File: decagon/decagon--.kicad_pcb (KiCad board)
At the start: 2 copper layers, 161.7 x 153.8 mm, 39 parts, among them J1 Conn_01x05_Pin, J10 Conn_01x05_Pin, J2 Conn_01x05_Pin, J3 Conn_01x05_Pin, J4 Conn_01x05_Pin, J5 Conn_01x05_Pin, J6 Conn_01x05_Pin, J7 Conn_01x05_Pin, J8 Conn_01x05_Pin, J9 Conn_01x05_Pin

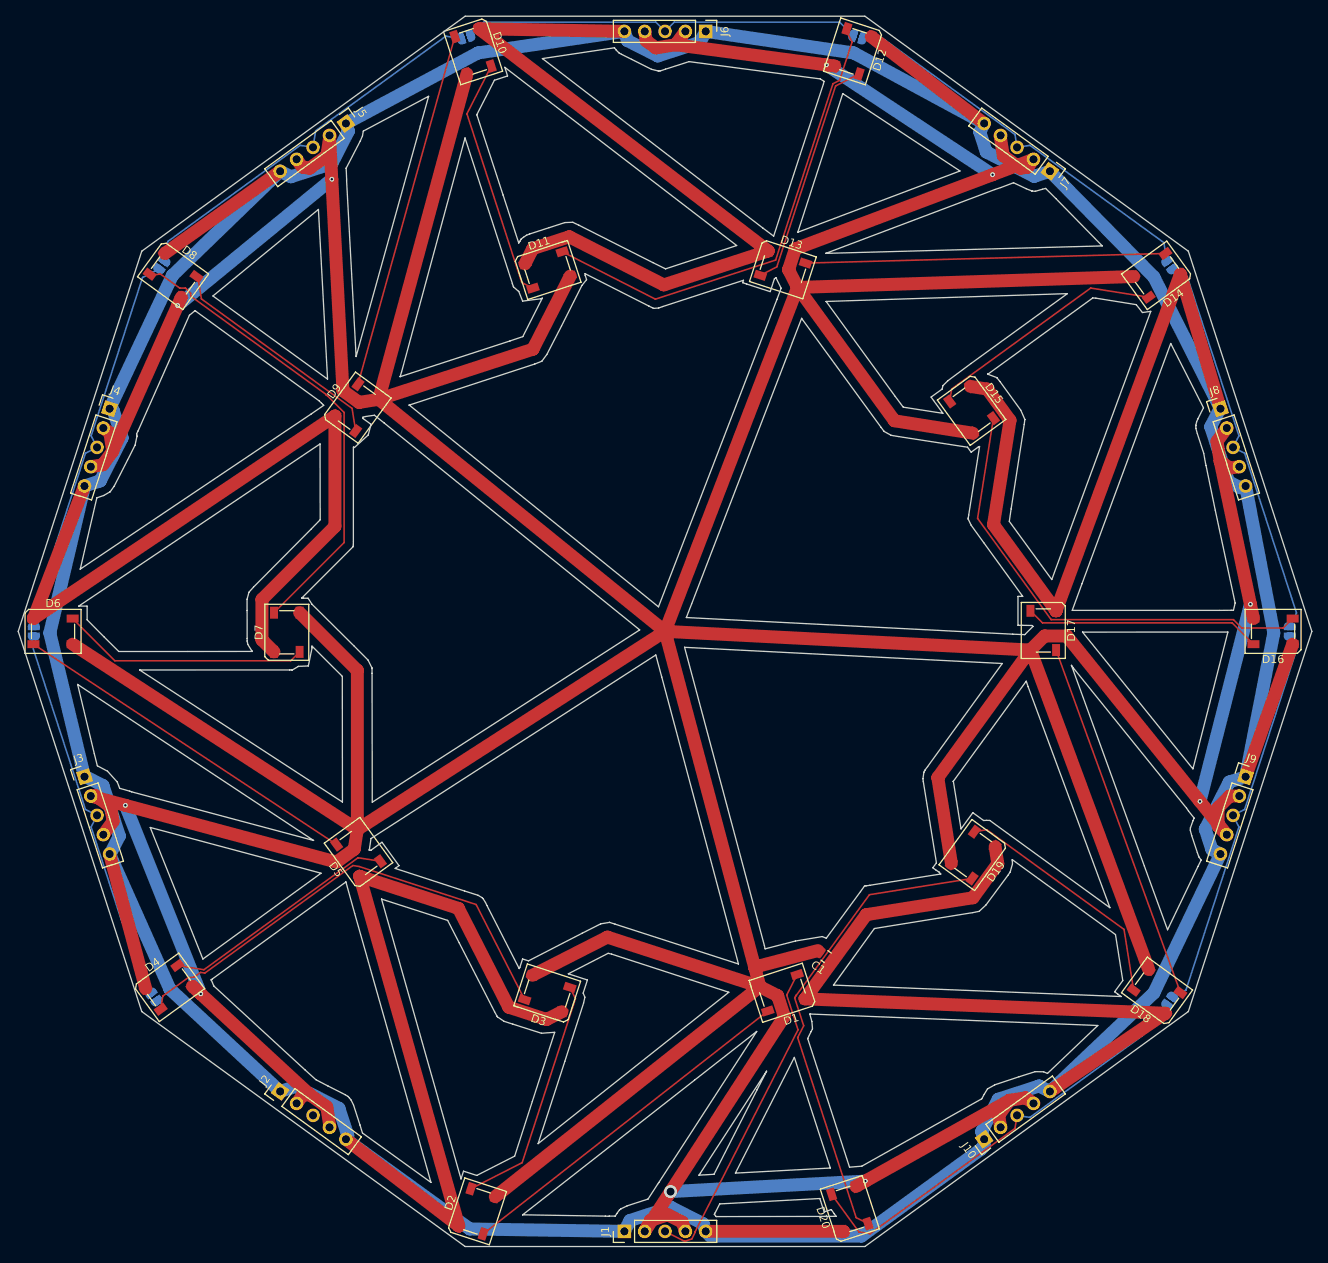
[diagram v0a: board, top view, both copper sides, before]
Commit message: fixed unconnected jumper wire
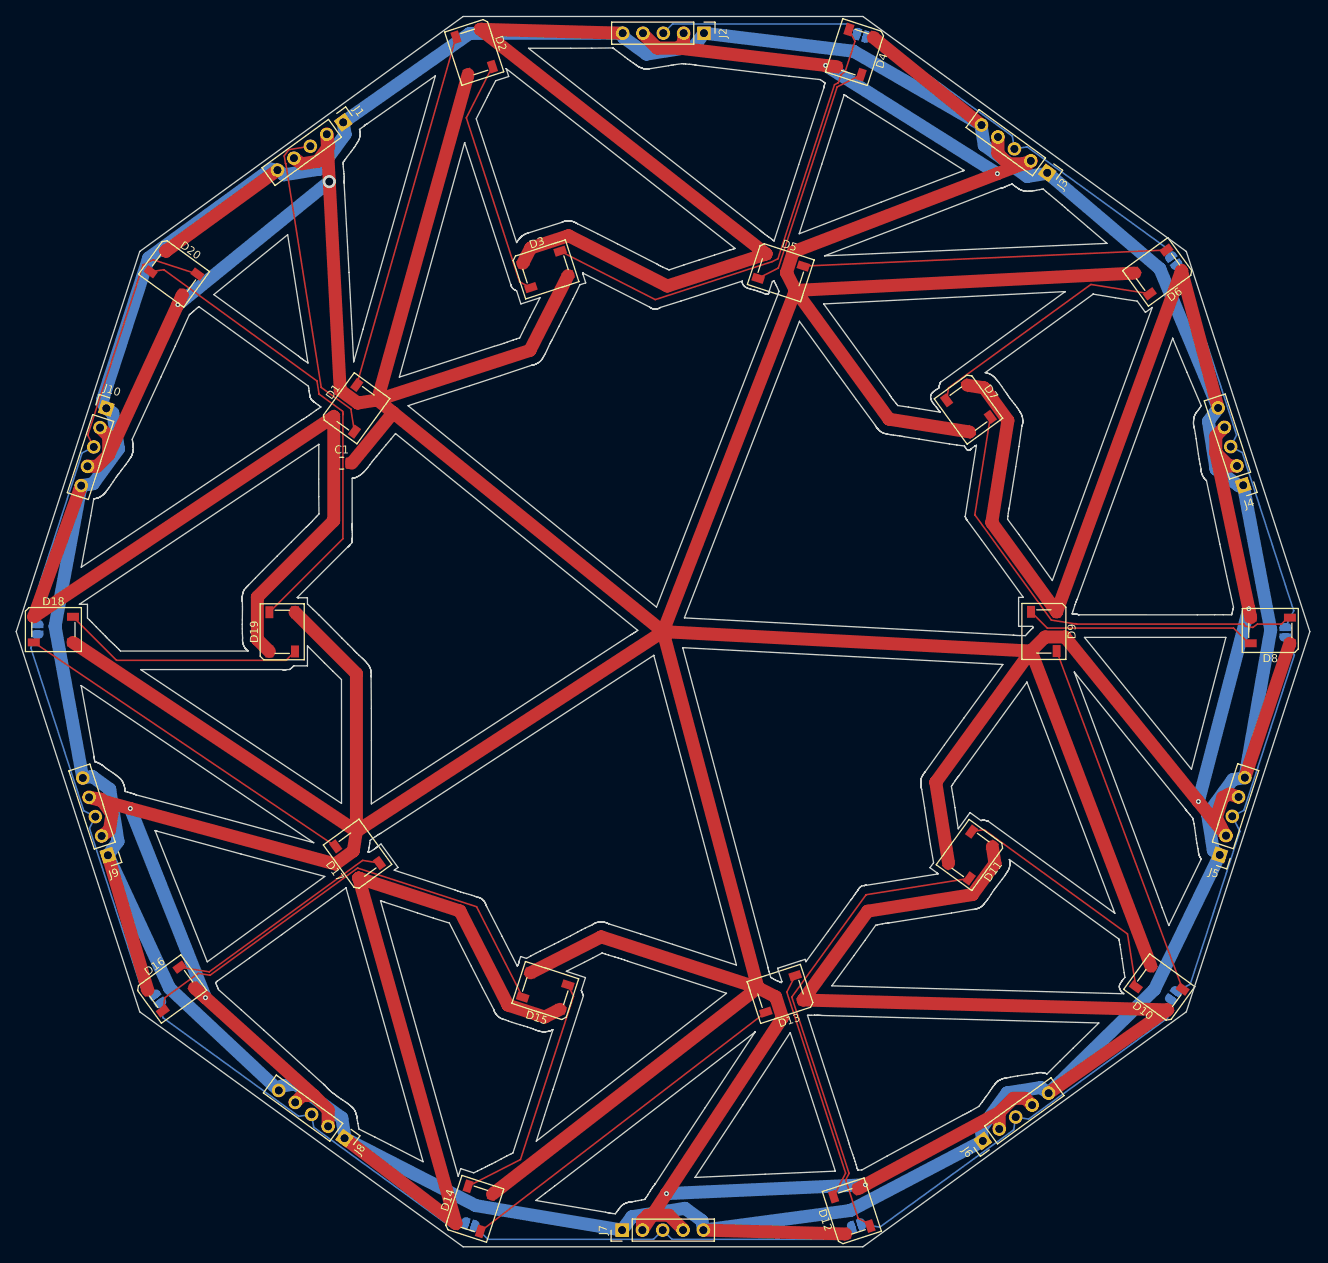
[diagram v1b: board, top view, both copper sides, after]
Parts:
- moved JP2 149.8 mm to (213.9, 53.7), turned to 126 degrees
- moved JP1 149.3 mm to (174.9, 25.6), turned to 162 degrees
- moved JP8 149.0 mm to (71.9, 99.8), turned to -90 degrees
- moved JP4 148.9 mm to (213.9, 145.6), turned to 54 degrees
- moved JP7 148.8 mm to (86.9, 146.0), turned to -54 degrees
- moved JP5 148.6 mm to (174.2, 174.4), turned to 18 degrees
- moved JP6 148.5 mm to (125.9, 174.2), turned to -18 degrees
- moved JP3 147.8 mm to (227.9, 100.2), turned to 90 degrees
- moved D6 145.3 mm to (212.0, 55.1), turned to -144 degrees
- moved D18 145.2 mm to (73.9, 99.9), turned to 0 degrees
- moved D10 145.1 mm to (212.1, 144.7), turned to 144 degrees
- moved D12 145.0 mm to (173.7, 172.6), turned to 108 degrees
- moved D4 145.0 mm to (174.1, 27.7), turned to -108 degrees
- moved D2 144.9 mm to (126.5, 27.6), turned to -72 degrees
- moved D16 144.8 mm to (88.6, 144.8), turned to 36 degrees
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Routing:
- net Net-(J2-Pin_3): track 0.00 -> 25.2 mm
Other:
- outline, holes or cut-outs redrawn
